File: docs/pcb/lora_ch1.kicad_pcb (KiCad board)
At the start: 2 copper layers, 69 x 34.5 mm, 42 parts

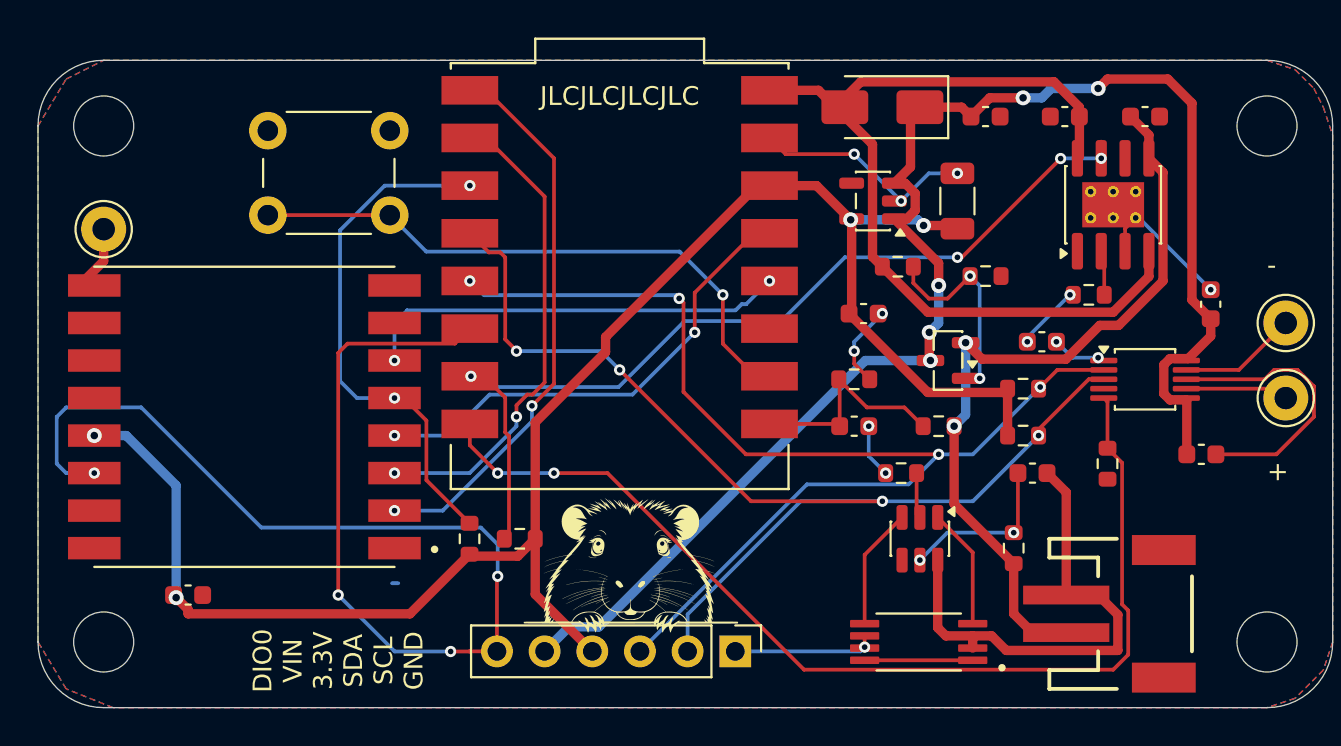
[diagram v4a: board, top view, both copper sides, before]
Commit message: PCB rework, added DIO1 connection to GPIO3, changed DIO0 location to GPIO2. Changed the charging controller from TP4056 to BQ24075RGT.
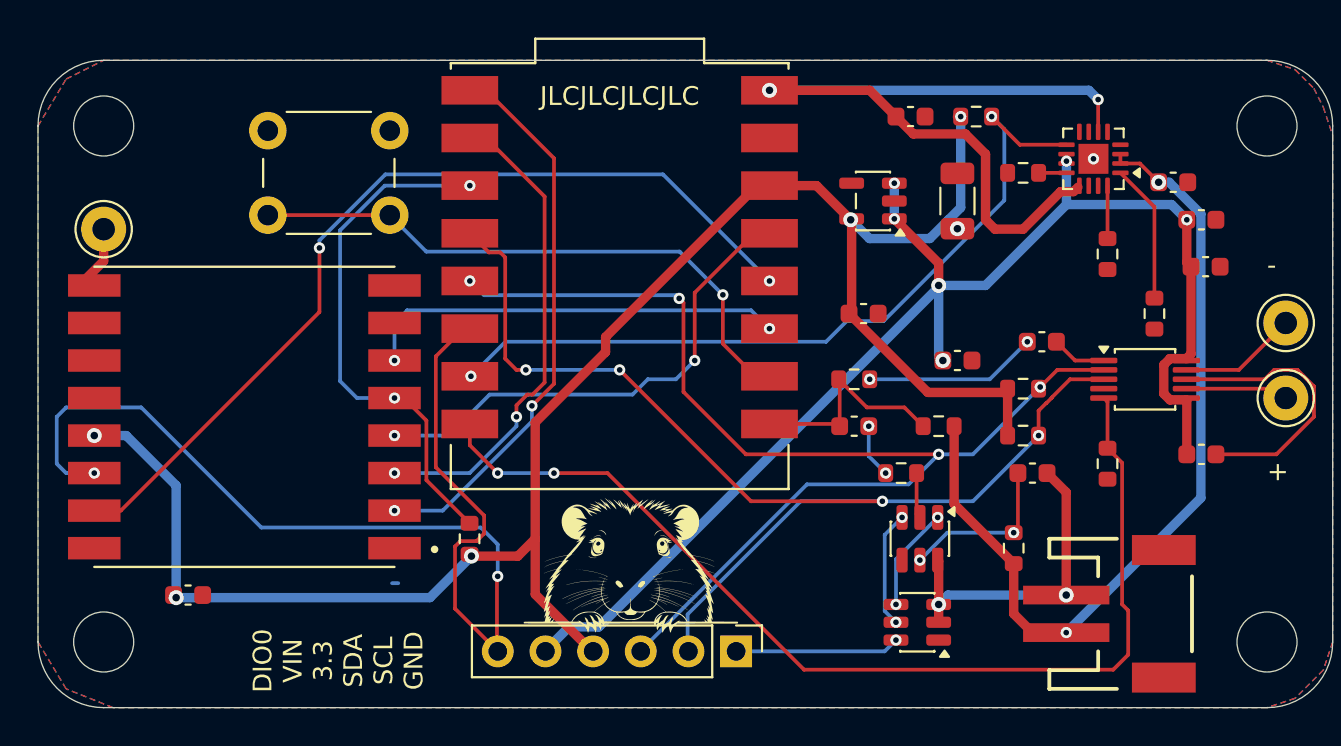
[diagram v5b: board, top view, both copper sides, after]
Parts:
- removed C3, C4: 10uF, PCM_SparkFun-Capacitor:C_0603_1608Metric
- removed MOSFET1: AO3401A, Package_TO_SOT_SMD:SOT-23
- removed R1: 2.0k, PCM_SparkFun-Resistor:R_0603_1608Metric
- removed SSD1: SS14, Diode_SMD:D_SMA
- added C12: 4.7uF, PCM_SparkFun-Capacitor:C_0603_1608Metric, F.Cu at (121.5, 63.0)
- added C13: 4.7uF, PCM_SparkFun-Capacitor:C_0603_1608Metric, F.Cu at (135.5, 66.5)
- added C14: 4.7uF, PCM_SparkFun-Capacitor:C_0603_1608Metric, F.Cu at (124.0, 76.0)
- added R13: 12k, PCM_SparkFun-Resistor:R_0603_1608Metric, F.Cu at (134.5, 73.5)
- BMS1: footprint FS8205A:SOP65P640X120-8N -> Package_TO_SOT_SMD:SOT-23-6
- C7: value 100nF -> 0.1uF
- CHRG1: value TP4056-42-ESOP8 -> BQ24075RGT; footprint Package_SO:SOIC-8-1EP_3.9x4.9mm_P1.27mm_EP2.41x3.3mm_ThermalVias -> Package_DFN_QFN:VQFN-16-1EP_3x3mm_P0.5mm_EP1.6x1.6mm
- R10: value 100k -> 1.8k
- R12: value 10k -> 12k
- R9: value 10k -> 1.8k
- moved R12 33.1 mm to (125.0, 63.0)
- moved C5 12.7 mm to (137.0, 68.5)
- moved R9 11.2 mm to (132.0, 70.3), turned to -90 degrees
- moved R10 5.85 mm to (127.5, 66.0), turned to 0 degrees
- moved CHRG1 2.67 mm to (131.2, 65.2), turned to 180 degrees
- moved C11 2.02 mm to (137.2, 71.0), turned to 0 degrees
- moved BMS1 1.05 mm to (121.9, 90.0)
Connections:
- CHRG1 pad 1: GND -> Net-(CHRG1-TS)
- CHRG1 pad 2: Net-(CHRG1-PROG) -> BATT_PLUS
- CHRG1 pad 3: GND -> BATT_PLUS
- CHRG1 pad 4: V_USB -> GND
- CHRG1 pad 5: BATT_PLUS -> GND
- CHRG1 pad 6: unconnected-(CHRG1-~{STDBY}-Pad6) -> V_USB
- CHRG1 pad 7: CHRG -> unconnected-(CHRG1-~{PGOOD}-Pad7)
- CHRG1 pad 8: V_USB -> GND
- CHRG1 pad 9: GND -> CHRG
- ESP1 pad 2: unconnected-(ESP1-GPIO2-Pad2) -> LORA_RST
- ESP1 pad 3: LORA_RST -> LORA_DIO1
- HAPTIC1 pad 4: unconnected-(HAPTIC1-IN/TRIG-Pad4) -> GND
- LORA1 pad 15: unconnected-(LORA1-DIO1-Pad15)_1 -> LORA_DIO1
- R10 pad 2: Net-(MOSFET1-G) -> Net-(CHRG1-ILIM)
- R12 pad 1: CHRG -> 3.3V
- R12 pad 2: 3.3V -> CHRG
- R9 pad 1: V_USB -> Net-(CHRG1-ISET)
- R9 pad 2: Net-(MOSFET1-G) -> GND
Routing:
- net LORA_DIO1: track 0.00 -> 48.0 mm, vias 0 -> 2
- net GND: track 54.6 -> 37.5 mm, vias 11 -> 6
- net Net-(MOSFET1-G): track 11.2 -> 0.00 mm, vias 2 -> 0
- net V_IN: track 82.0 -> 72.6 mm, vias 5 -> 6
- net LORA_DIO0: track 67.3 -> 58.5 mm, vias 4 -> 2
- net CHRG: track 49.8 -> 41.7 mm, vias 4 -> 2
- net Net-(CHRG1-TS): track 0.00 -> 7.43 mm
- net BATT_MINUS: track 26.4 -> 19.0 mm, vias 0 -> 2
- net 3.3V: track 93.8 -> 99.8 mm, vias 4 -> 6
- net Net-(BMS1-Pad1): track 5.76 -> 0.00 mm
- net V_USB: track 47.5 -> 42.0 mm, vias 0 -> 2
- net BATT_PLUS: track 41.6 -> 45.7 mm
- net Net-(CHRG1-ISET): track 0.00 -> 2.81 mm
- net Net-(CHRG1-PROG): track 2.39 -> 0.00 mm
- net Net-(CHRG1-ILIM): track 0.00 -> 1.49 mm
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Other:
- board text added: "DIO0 VIN 3.3 SDA SCL GND"
- board text removed: "DIO0 VIN 3.3V SDA SCL GND"
